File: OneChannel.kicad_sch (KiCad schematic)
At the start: 55 parts, among them Q201 NDFPD1N150CG, U201 OPA2156xD, U202 OPA2156xD, U203 OPA2156xD, U204 OPA2156xD

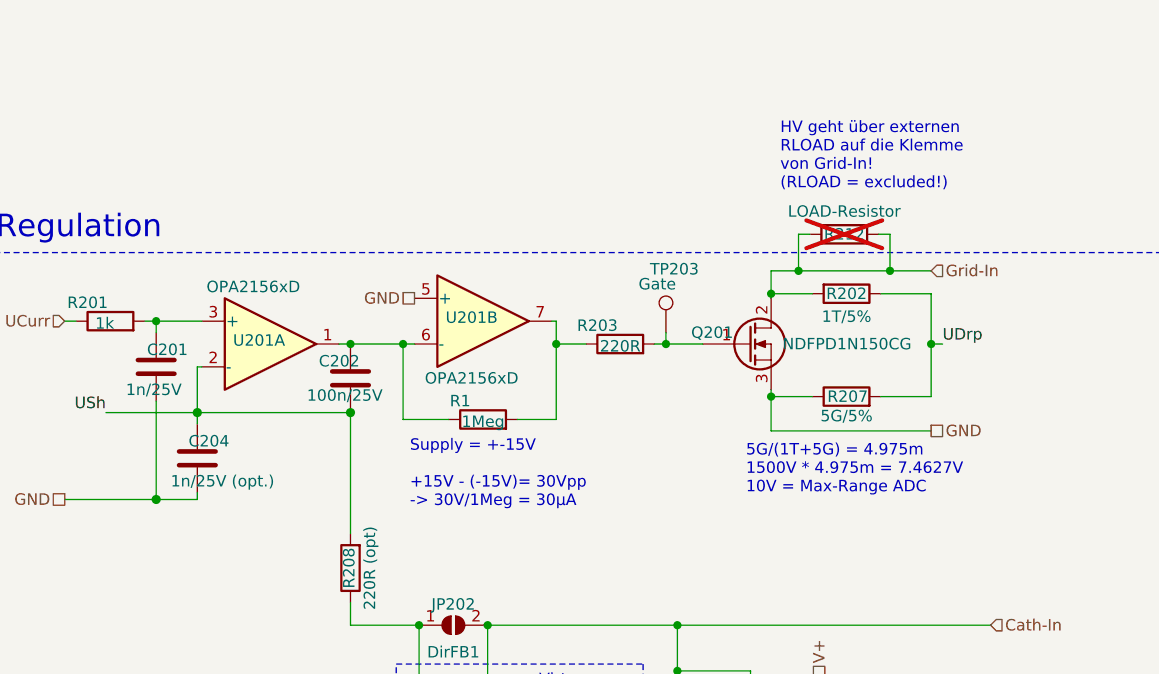
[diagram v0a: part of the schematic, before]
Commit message: Added option to invert FET-Gate voltage
Added JP206 (3Pad Solder Jumper) and JP204 (2Pad Solder Jumper)
These using the, until now, unused second OpAmp of U201.

--> Jumpers that allow to invert the FET-Gate Voltage

FET-Gate Voltage acts as Grid-Regulation (inverting):
- Close JP206 Pins 2 with 3
- Close JP204
- Use R215 = 1Meg

FET-Gate Voltage acts as Cath-Regulation (non inverting):
- Close JP206 Pins 2 with 1
- Open  JP204
- Use R215 = 0R (Short-Circuit)

Candidate for V1.2
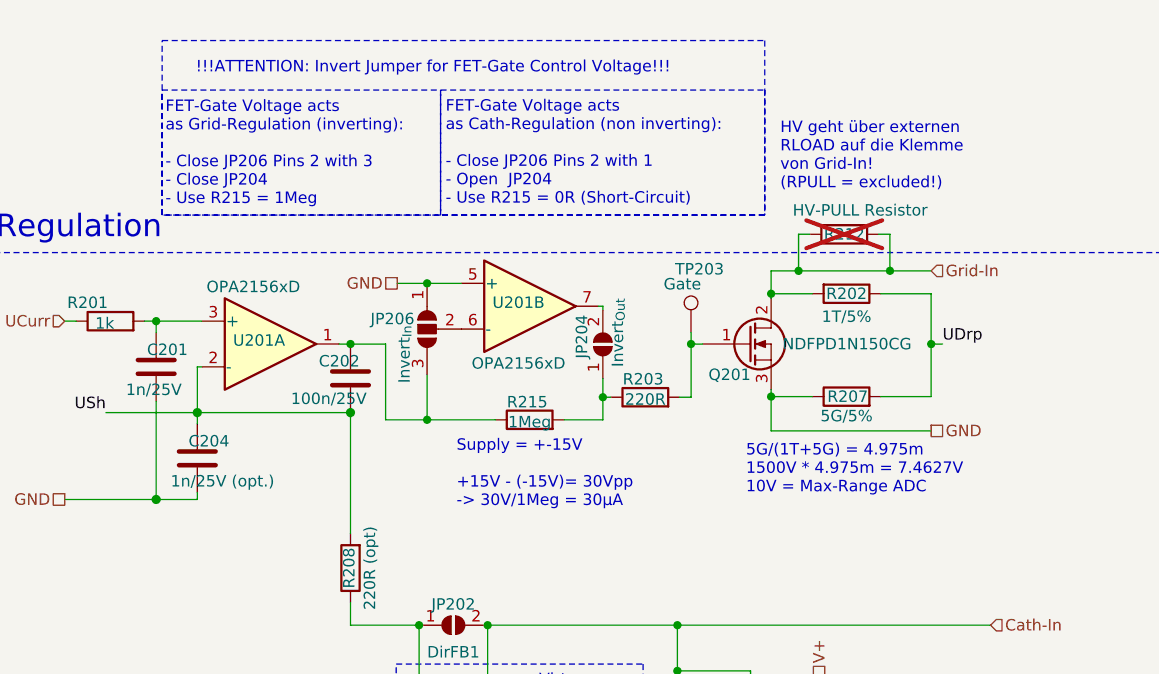
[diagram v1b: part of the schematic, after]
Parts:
- added JP204: Invert_{Out}, Jumper:SolderJumper-2_P1.3mm_Open_RoundedPad1.0x1.5mm, symbol Jumper:SolderJumper_2_Open
- added JP206: Invert_{In}, Jumper:SolderJumper-3_P1.3mm_Open_RoundedPad1.0x1.5mm, symbol Jumper:SolderJumper_3_Open
- R212: value LOAD-Resistor -> HV-PULL Resistor
- renumbered R1 to R215
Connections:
- net GND: now also JP206.1 (A)
- net at C202.2, R215.1, U201.1: now also JP206.3 (B); no longer U201.6 (-)
- net at R203.1, R215.2: now also JP204.1 (A); no longer U201.7
- new net: JP204.2 (B), U201.7
- new net: JP206.2 (C), U201.6 (-)
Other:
- note added: "!!!ATTENTION: Invert Jumper for FET-Gate Control Voltage!!!"
- note added: "FET-Gate Voltage acts as Cath-Regulation (non inverting): - Close JP206 Pins 2 with 1 - Open JP204 - Use R215 = 0R (Short-Circuit)"
- note added: "FET-Gate Voltage acts as Grid-Regulation (inverting): - Close JP206 Pins 2 with 3 - Close JP204 - Use R215 = 1Meg"
- note added: "HV geht über externen RLOAD auf die Klemme von Grid-In! (RPULL = excluded!)"
- note removed: "HV geht über externen RLOAD auf die Klemme von Grid-In! (RLOAD = excluded!)"
- moved on the sheet: R203, R215, TP203, U201B

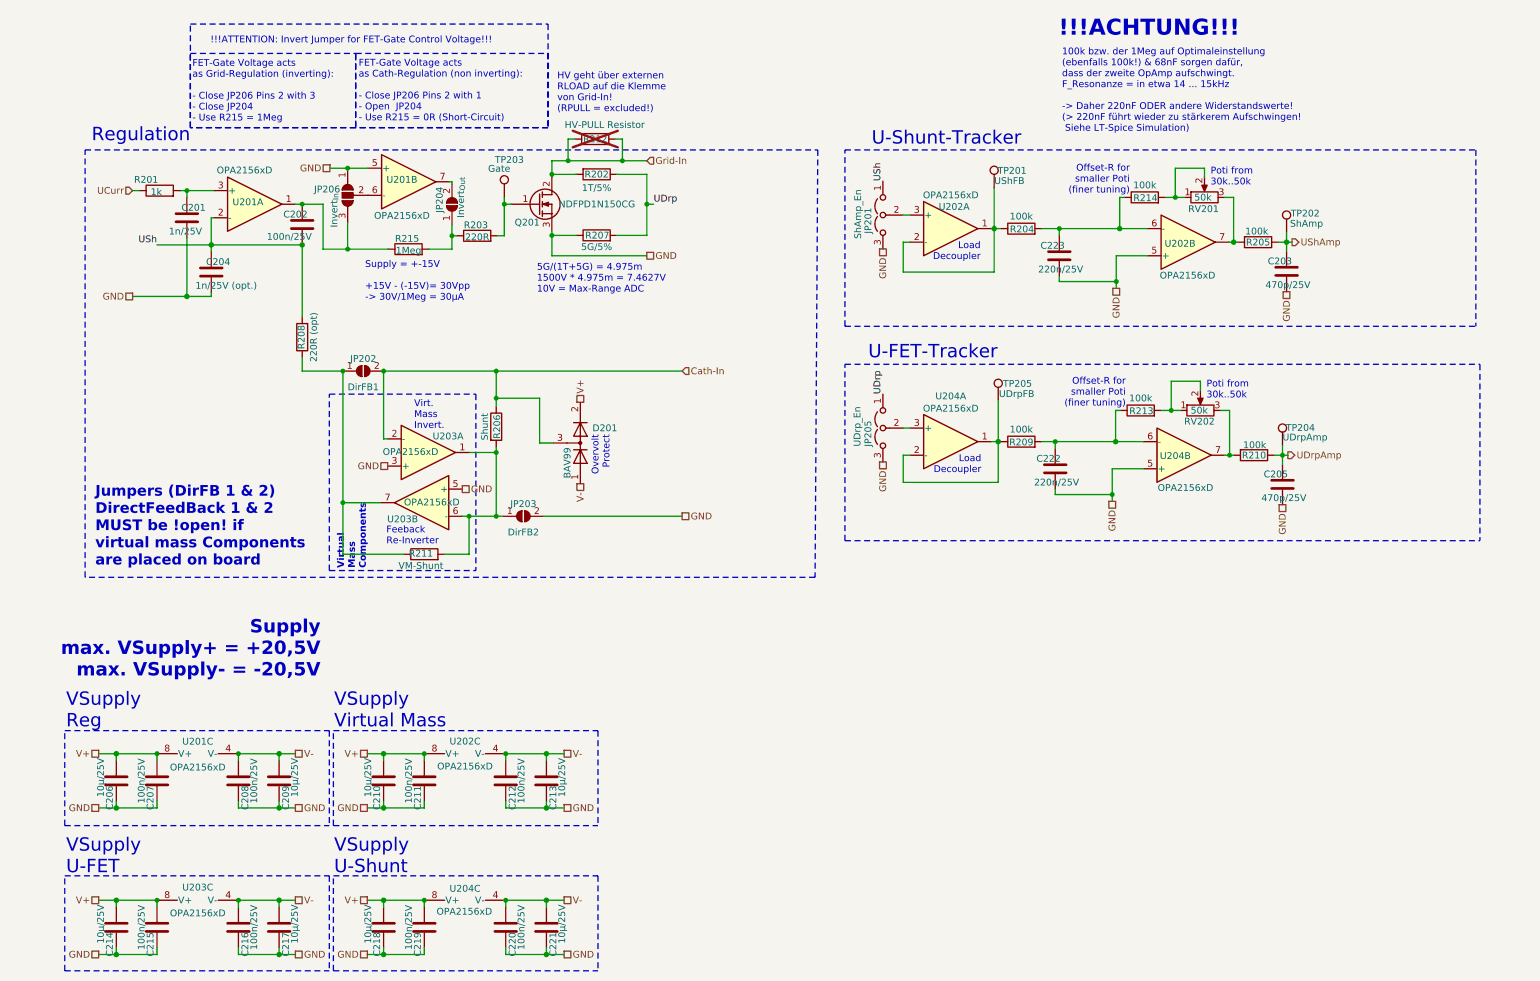
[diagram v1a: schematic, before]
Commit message: Added comments on UFET feedback loop
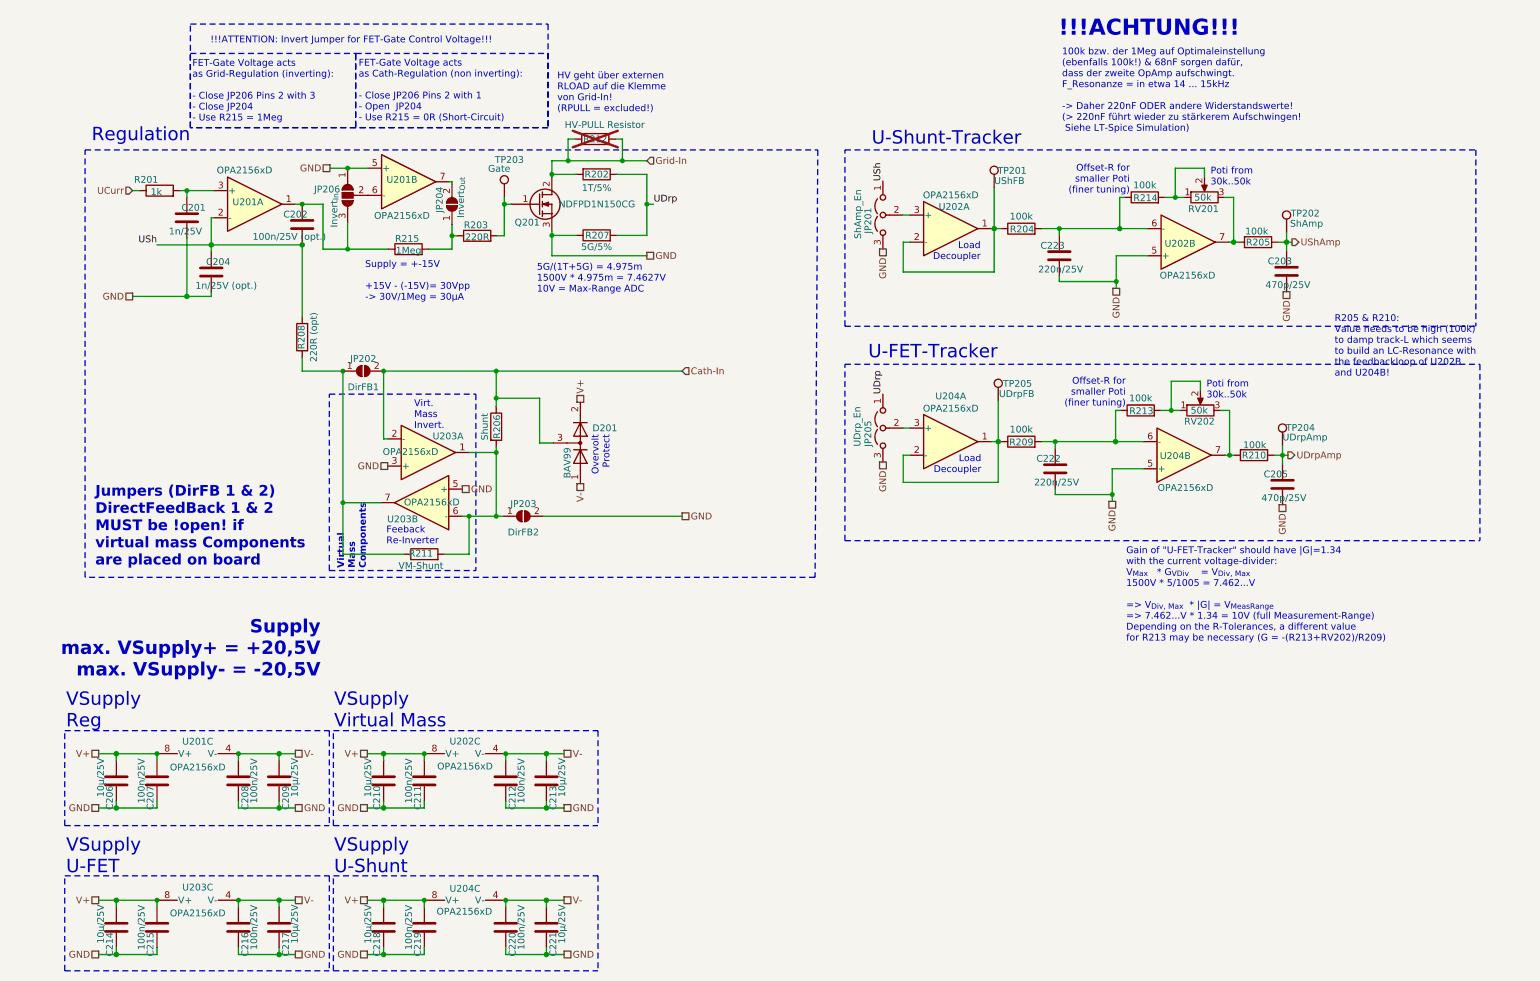
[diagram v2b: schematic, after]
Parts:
- C202: value 100n/25V -> 100n/25V (opt.)
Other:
- note added: "Gain of "U-FET-Tracker" should have |G|=1.34 with the current voltage-divider: V_{Max} * G_{VDiv} = V_{Div, Max} 1500V * 5/1005 = 7.462...V => V_{Div, Max} * |G| = V_{MeasRange} => 7.462...V * 1.34 = 10V (full Measurement-Range) Depending on the R-Tolerances, a different value for R213 may be necessary (G = -(R213+RV202)/R209)"
- note added: "R205 & R210: Value needs to be high (100k) to damp track-L which seems to build an LC-Resonance with the feedbackloop of U202B and U204B!"
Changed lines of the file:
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@@
 		)
 	)
+	(text "R205 & R210:\nValue needs to be high (100k)\nto damp track-L which seems\nto build an LC-Resonance with\nthe feedbackloop of U202B\nand U204B!"
+		(exclude_from_sim no)
+		(at 251.69 84.57 0)
+		(effects
+			(font
+				(size 1.27 1.27)
+			)
+			(justify left bottom)
+		)
+	)
 	(text "HV geht über externen\nRLOAD auf die Klemme\nvon Grid-In!\n(RPULL = excluded!)"
 		(exclude_from_sim no)
@@
 		)
 	)
+	(text "Gain of \"U-FET-Tracker\" should have |G|=1.34\nwith the current voltage-divider:\nV_{Max}   * G_{VDiv}    = V_{Div, Max}\n1500V * 5/1005 = 7.462...V\n\n=> V_{Div, Max}  * |G| = V_{MeasRange}\n=> 7.462...V * 1.34 = 10V (full Measurement-Range)\nDepending on the R-Tolerances, a different value\nfor R213 may be necessary (G = -(R213+RV202)/R209)"
+		(exclude_from_sim no)
+		(at 212.68 125.24 0)
+		(effects
+			(font
+				(size 1.27 1.27)
+			)
+			(justify left)
+		)
+	)
 	(text "!!!ACHTUNG!!!"
 		(exclude_from_sim no)
@@
 			)
 		)
-		(property "Value" "100n/25V"
+		(property "Value" "100n/25V (opt.)"
 			(at 56.01 58.15 0)
 			(effects
